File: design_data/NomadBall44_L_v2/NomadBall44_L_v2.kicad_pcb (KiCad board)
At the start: 2 copper layers, 149 x 96.5 mm, 58 parts, among them SW1 SW_Push, SW10 SW_Push, SW11 SW_Push, SW12 SW_Push, SW13 SW_Push, SW14 SW_Push, SW15 SW_Push, SW16 SW_Push, SW17 SW_Push, SW18 SW_Push, SW19 SW_Push, SW2 SW_Push, SW20 SW_Push, SW21 SW_Push, SW22 SW_Push, SW23 SW_Push, SW24 SW_SPDT, SW3 SW_Push, SW4 SW_Push, SW5 SW_Push, SW6 SW_Push, SW7 SW_Push, SW8 SW_Push, SW9 SW_Push, U1 XIAO-nRF52840-Plus-SMD

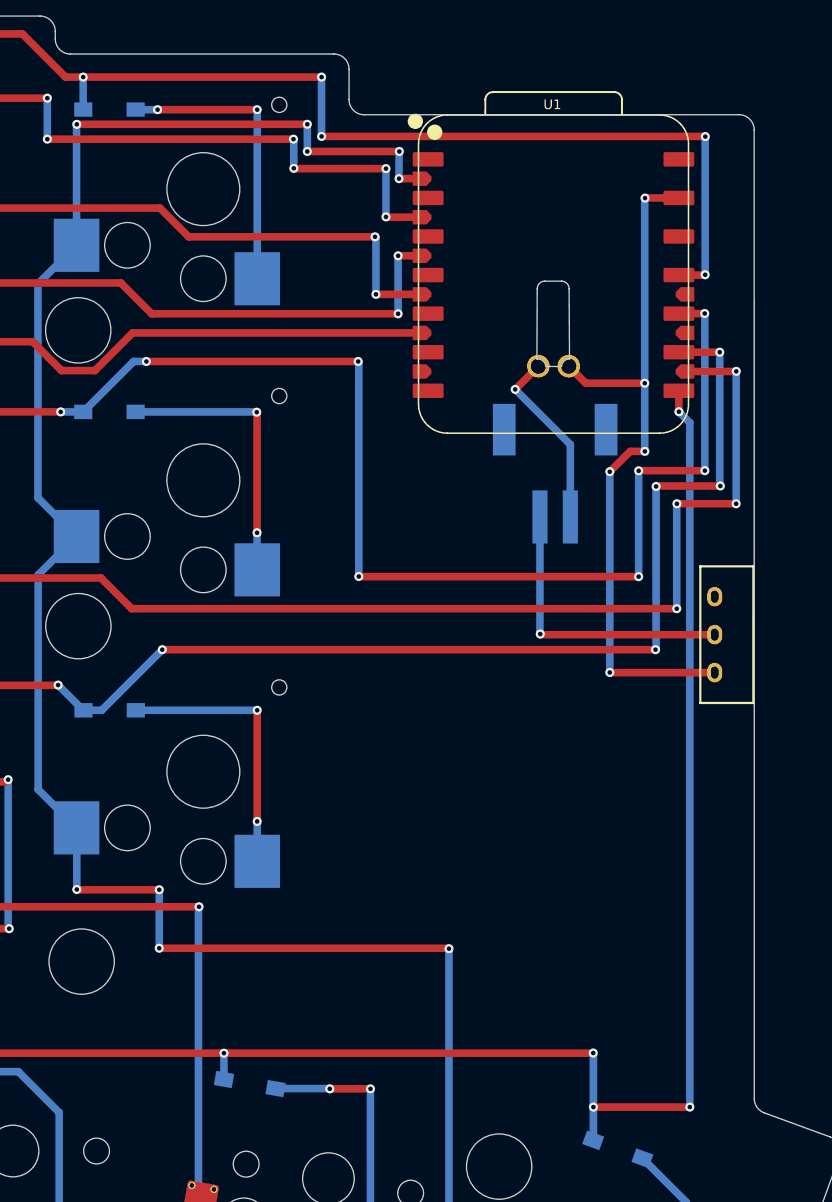
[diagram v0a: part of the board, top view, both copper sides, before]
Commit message: 左手基板のマイコンfootprintを変更し配線を修正
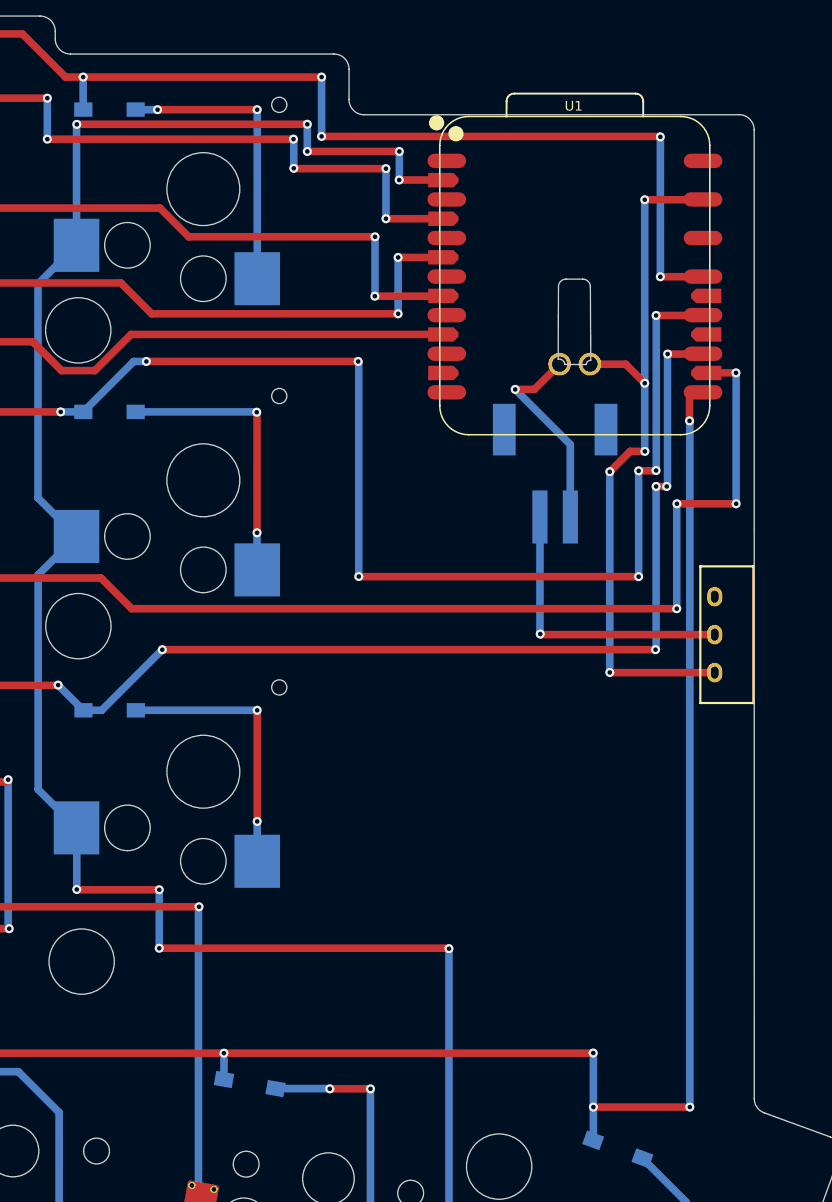
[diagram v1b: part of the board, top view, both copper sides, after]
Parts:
- U1: footprint NomadBall44:XIAO-nRF52840-Plus-ver2 -> NomadBall44:XIAO-nRF52840-Plus-ver3
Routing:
- net Row2: track 179.8 -> 175.0 mm
- net Row1: track 190.7 -> 188.0 mm
- net Row0: track 171.8 -> 169.2 mm
- net Col3: track 154.1 -> 155.7 mm
- net Col5: track 212.8 -> 211.3 mm
- net Col1: track 154.1 -> 155.6 mm
- net Col0: track 131.7 -> 133.3 mm
- net Bat: track 12.1 -> 13.5 mm
- net Col4: track 170.4 -> 171.8 mm
- net Col2: track 167.8 -> 169.1 mm
- net GND: track 47.4 -> 46.7 mm

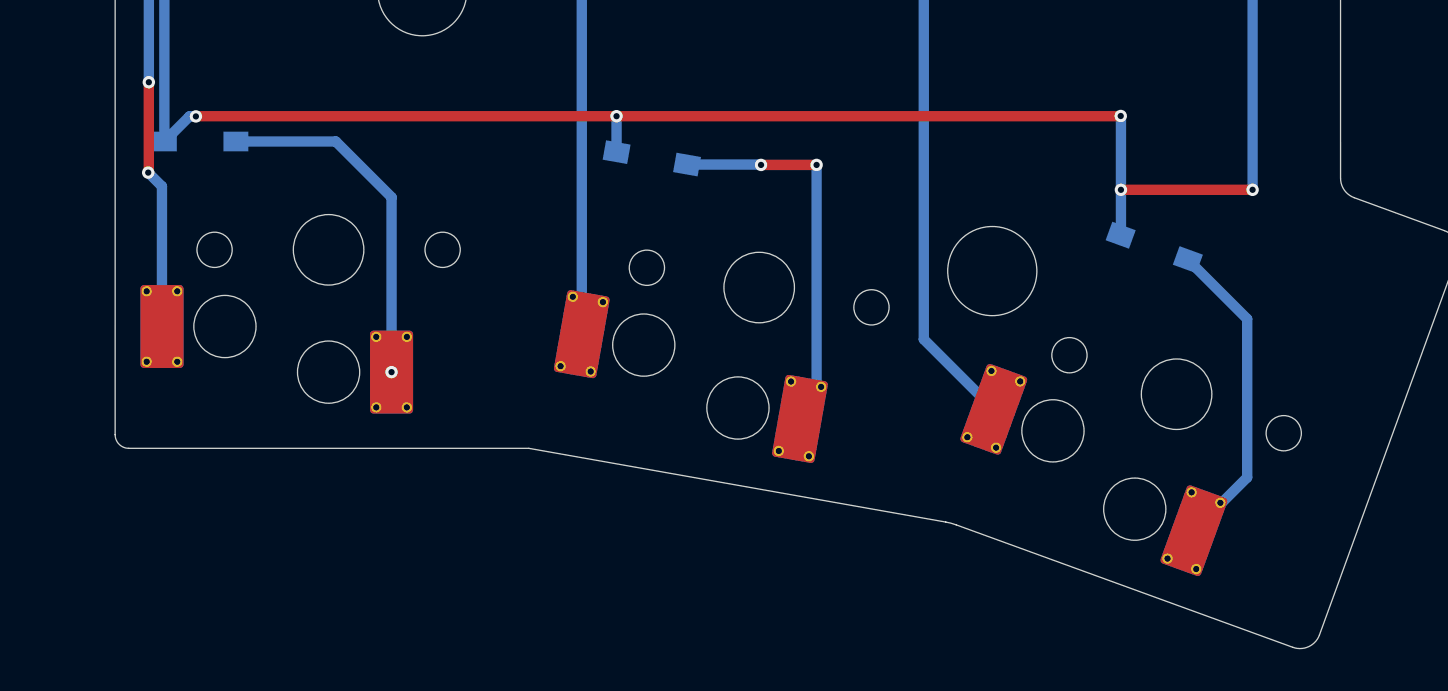
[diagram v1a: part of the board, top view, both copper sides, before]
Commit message: chocv1をchocv2に変更
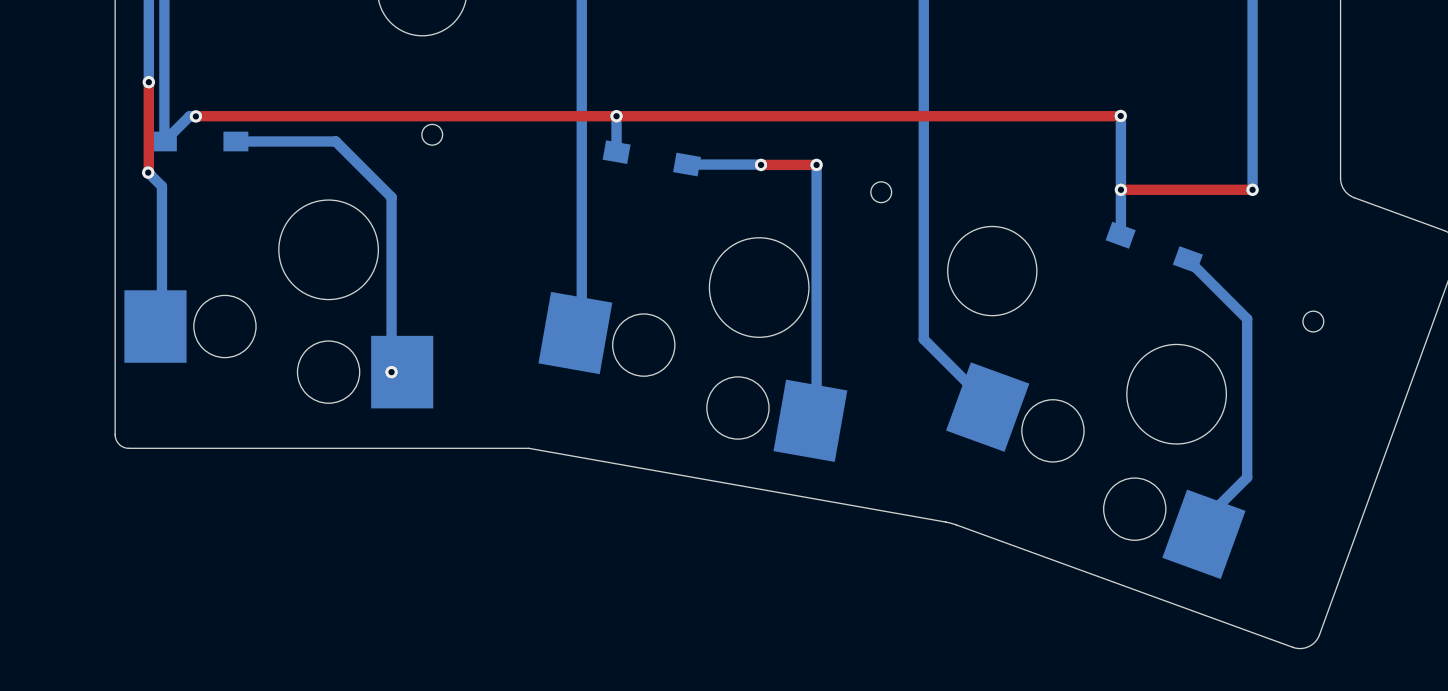
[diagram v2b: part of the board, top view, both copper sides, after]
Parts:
- SW19, SW20, SW21: footprint NomadBall44:Kailh_Choc_V1_Hotswap_thin_via -> NomadBall44:Choc_v2_Hotswap_1u

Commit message: キースイッチの配置を修正
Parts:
- renumbered SW6 to SW1, SW9 to SW10, SW8 to SW11, SW7 to SW12, SW18 to SW13, SW17 to SW14, SW16 to SW15, SW15 to SW16, SW14 to SW17, SW13 to SW18, SW23 to SW19, SW5 to SW2, SW22 to SW20, SW20 to SW22, SW19 to SW23, SW4 to SW3, SW3 to SW4, SW2 to SW5, SW1 to SW6, SW12 to SW7, SW11 to SW8, SW10 to SW9
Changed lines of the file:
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@@
 		(layer "F.Cu")
 		(at 181.384757 126.99)
-		(property "Reference" "SW22"
+		(property "Reference" "SW20"
 			(at 0.5 -5.5 180)
 			(layer "B.SilkS")
@@
 		(layer "F.Cu")
 		(at 162.284757 113.419999)
-		(property "Reference" "SW17"
+		(property "Reference" "SW14"
 			(at 0.5 -5.5 180)
 			(layer "B.SilkS")
@@
 		(layer "F.Cu")
 		(at 181.384757 107.789999)
-		(property "Reference" "SW16"
+		(property "Reference" "SW15"
 			(at 0.5 -5.5 180)
 			(layer "B.SilkS")
@@
 		(layer "F.Cu")
 		(at 247.190659 134.214444 -10)
-		(property "Reference" "SW20"
+		(property "Reference" "SW22"
 			(at 0.5 -5.5 170)
 			(layer "B.SilkS")
@@
 		)
 		(fp_line
-			(start -6.250001 6)
+			(start -6.250002 6)
 			(end -6.25 1.4)
 			(stroke
@@
 		(fp_line
 			(start -1.3 7.99)
-			(end -1.300001 3.6)
+			(end -1.300002 3.6)
 			(stroke
 				(width 0.15)
@@
 		)
 		(fp_line
-			(start 1.7 7.820001)
+			(start 1.7 7.820003)
 			(end 1.7 3.99)
 			(stroke
@@
 		)
 		(fp_line
-			(start 1.85 7.660001)
+			(start 1.85 7.660002)
 			(end 1.85 4.13)
 			(stroke
@@
 		(layer "F.Cu")
 		(at 143.10132 94.239999)
-		(property "Reference" "SW12"
+		(property "Reference" "SW7"
 			(at 0.5 -5.5 180)
 			(layer "B.SilkS")
@@
 		(layer "F.Cu")
 		(at 267.324757 139.359999 -20)
-		(property "Reference" "SW19"
+		(property "Reference" "SW23"
 			(at 0.5 -5.5 160)
 			(layer "B.SilkS")
@@
 		(fp_line
 			(start 0.95 8.2)
-			(end 0.95 3.600001)
+			(end 0.95 3.600002)
 			(stroke
 				(width 0.15)
@@
 		(layer "F.Cu")
 		(at 219.774757 85.989999)
-		(property "Reference" "SW8"
+		(property "Reference" "SW11"
 			(at 0.5 -5.5 180)
 			(layer "B.SilkS")
@@
 		(layer "F.Cu")
 		(at 200.584757 64.459999)
-		(property "Reference" "SW3"
+		(property "Reference" "SW4"
 			(at 0.5 -5.5 180)
 			(layer "B.SilkS")
@@
 		(layer "F.Cu")
 		(at 238.954132 107.414999)
-		(property "Reference" "SW13"
+		(property "Reference" "SW18"
 			(at 0.5 -5.5 180)
 			(layer "B.SilkS")
@@
 		(layer "F.Cu")
 		(at 219.774757 66.799999)
-		(property "Reference" "SW2"
+		(property "Reference" "SW5"
 			(at 0.5 -5.5 180)
 			(layer "B.SilkS")
@@
 		(layer "F.Cu")
 		(at 181.384757 88.644999)
-		(property "Reference" "SW10"
+		(property "Reference" "SW9"
 			(at 0.5 -5.5 180)
 			(layer "B.SilkS")
@@
 		(layer "F.Cu")
 		(at 143.10132 75.034999)
-		(property "Reference" "SW6"
+		(property "Reference" "SW1"
 			(at 0.5 -5.5 180)
 			(layer "B.SilkS")
@@
 		(layer "F.Cu")
 		(at 162.284757 75.034999)
-		(property "Reference" "SW5"
+		(property "Reference" "SW2"
 			(at 0.5 -5.5 180)
 			(layer "B.SilkS")
@@
 		(layer "F.Cu")
 		(at 200.584757 83.649999)
-		(property "Reference" "SW9"
+		(property "Reference" "SW10"
 			(at 0.5 -5.5 180)
 			(layer "B.SilkS")
@@
 		(layer "F.Cu")
 		(at 181.384757 69.449999)
-		(property "Reference" "SW4"
+		(property "Reference" "SW3"
 			(at 0.5 -5.5 180)
 			(layer "B.SilkS")
@@
 		(layer "F.Cu")
 		(at 143.10132 113.419999)
-		(property "Reference" "SW18"
+		(property "Reference" "SW13"
 			(at 0.5 -5.5 180)
 			(layer "B.SilkS")
@@
 		(layer "F.Cu")
 		(at 162.284757 132.469999)
-		(property "Reference" "SW23"
+		(property "Reference" "SW19"
 			(at 0.5 -5.5 180)
 			(layer "B.SilkS")
@@
 		(layer "F.Cu")
 		(at 238.954132 88.224999)
-		(property "Reference" "SW7"
+		(property "Reference" "SW12"
 			(at 0.5 -5.5 180)
 			(layer "B.SilkS")
@@
 		(layer "F.Cu")
 		(at 238.954132 69.049999)
-		(property "Reference" "SW1"
+		(property "Reference" "SW6"
 			(at 0.5 -5.5 180)
 			(layer "B.SilkS")
@@
 		(layer "F.Cu")
 		(at 162.284757 94.239999)
-		(property "Reference" "SW11"
+		(property "Reference" "SW8"
 			(at 0.5 -5.5 180)
 			(layer "B.SilkS")
@@
 		(layer "F.Cu")
 		(at 200.584757 102.814999)
-		(property "Reference" "SW15"
+		(property "Reference" "SW16"
 			(at 0.5 -5.5 180)
 			(layer "B.SilkS")
@@
 		(layer "F.Cu")
 		(at 219.774757 105.184999)
-		(property "Reference" "SW14"
+		(property "Reference" "SW17"
 			(at 0.5 -5.5 180)
 			(layer "B.SilkS")

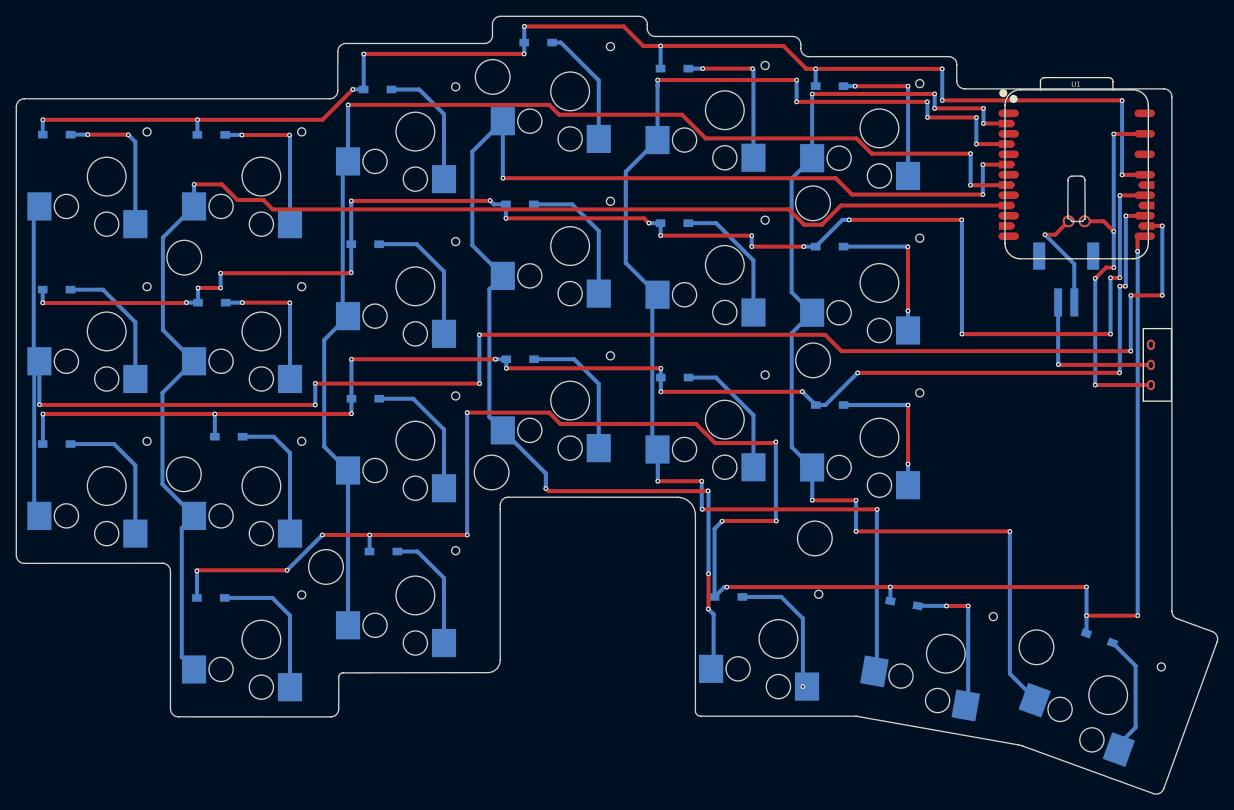
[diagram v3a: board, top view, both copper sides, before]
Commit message: ダイオードの配置を修正
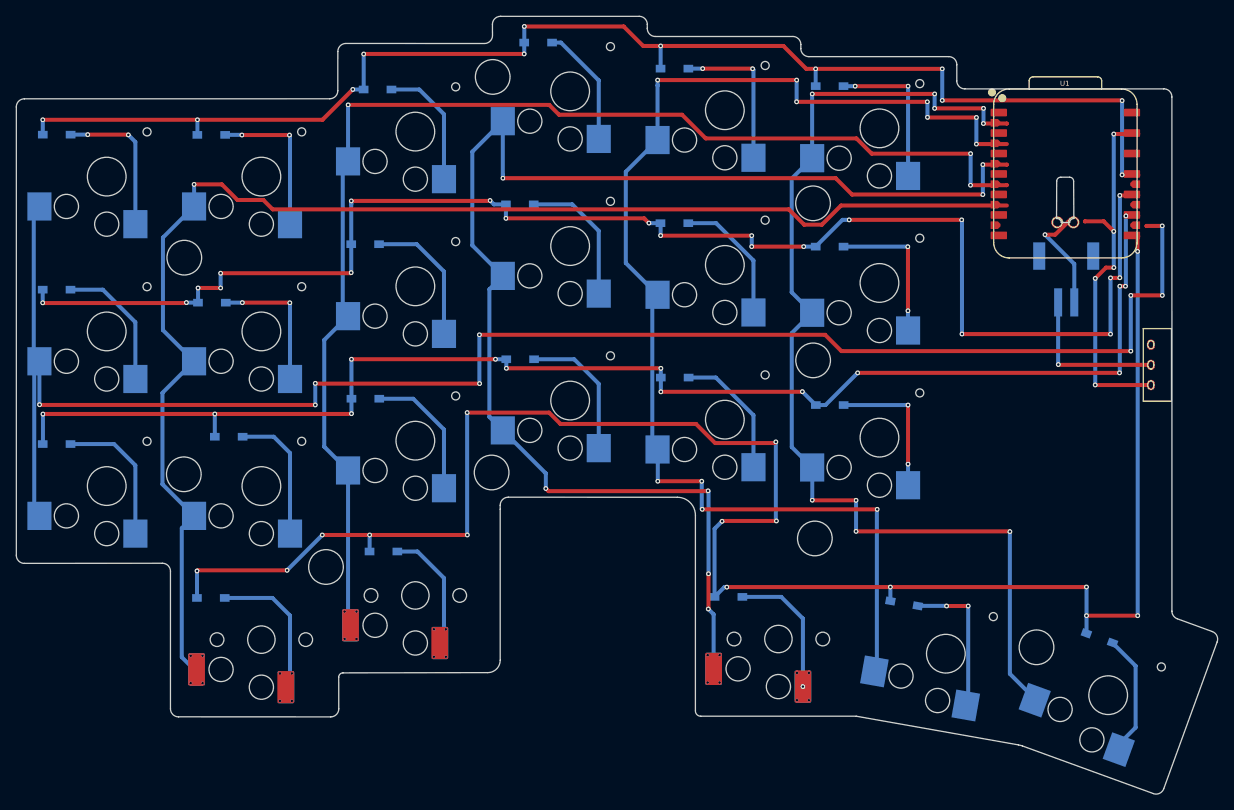
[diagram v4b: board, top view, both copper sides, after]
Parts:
- SW19, SW20, SW21: footprint NomadBall44:Choc_v2_Hotswap_1u -> NomadBall44:Kailh_Choc_V1_Hotswap_thin_via
- U1: footprint NomadBall44:XIAO-nRF52840-Plus-ver3 -> NomadBall44:XIAO-nRF52840-Plus-ver2
- renumbered D6 to D1, D9 to D10, D8 to D11, D7 to D12, D18 to D13, D17 to D14, D16 to D15, D15 to D16, D14 to D17, D13 to D18, D23 to D19, D5 to D2, D22 to D20, D20 to D22, D19 to D23, D4 to D3, D3 to D4, D2 to D5, D1 to D6, D12 to D7, D11 to D8, D10 to D9
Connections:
- SW1 pad 1: Col5 -> Col0
- SW10 pad 1: Col2 -> Col3
- SW11 pad 1: Col1 -> Col4
- SW12 pad 1: Col0 -> Col5
- SW13 pad 1: Col5 -> Col0
- SW14 pad 1: Col4 -> Col1
- SW15 pad 1: Col3 -> Col2
- SW16 pad 1: Col2 -> Col3
- SW17 pad 1: Col1 -> Col4
- SW18 pad 1: Col0 -> Col5
- SW19 pad 1: Col4 -> Col0
- SW2 pad 1: Col4 -> Col1
- SW20 pad 1: Col3 -> Col1
- SW22 pad 1: Col1 -> Col3
- SW23 pad 1: Col0 -> Col4
- SW3 pad 1: Col3 -> Col2
- SW4 pad 1: Col2 -> Col3
- SW5 pad 1: Col1 -> Col4
- SW6 pad 1: Col0 -> Col5
- SW7 pad 1: Col5 -> Col0
- SW8 pad 1: Col4 -> Col1
- SW9 pad 1: Col3 -> Col2
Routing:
- net Col5: track 211.3 -> 0.00 mm, vias 9 -> 0
- net Col0: track 133.3 -> 344.5 mm, vias 9 -> 18

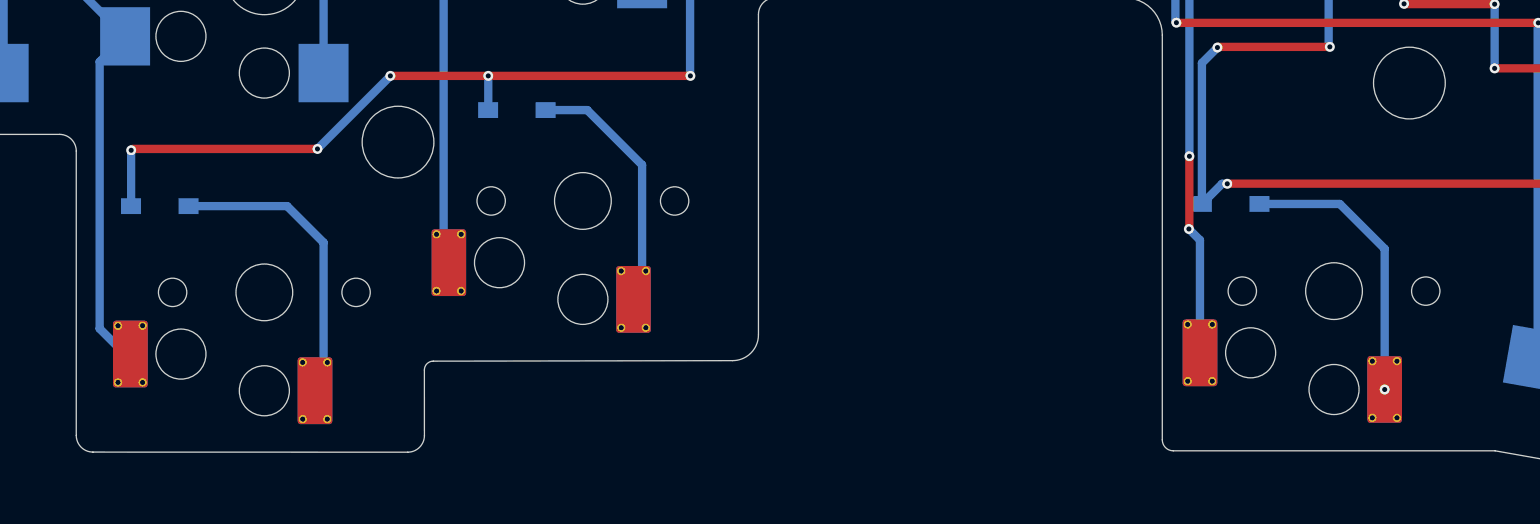
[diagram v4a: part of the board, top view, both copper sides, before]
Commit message: キースイッチをchocv1からchocv2へ変更
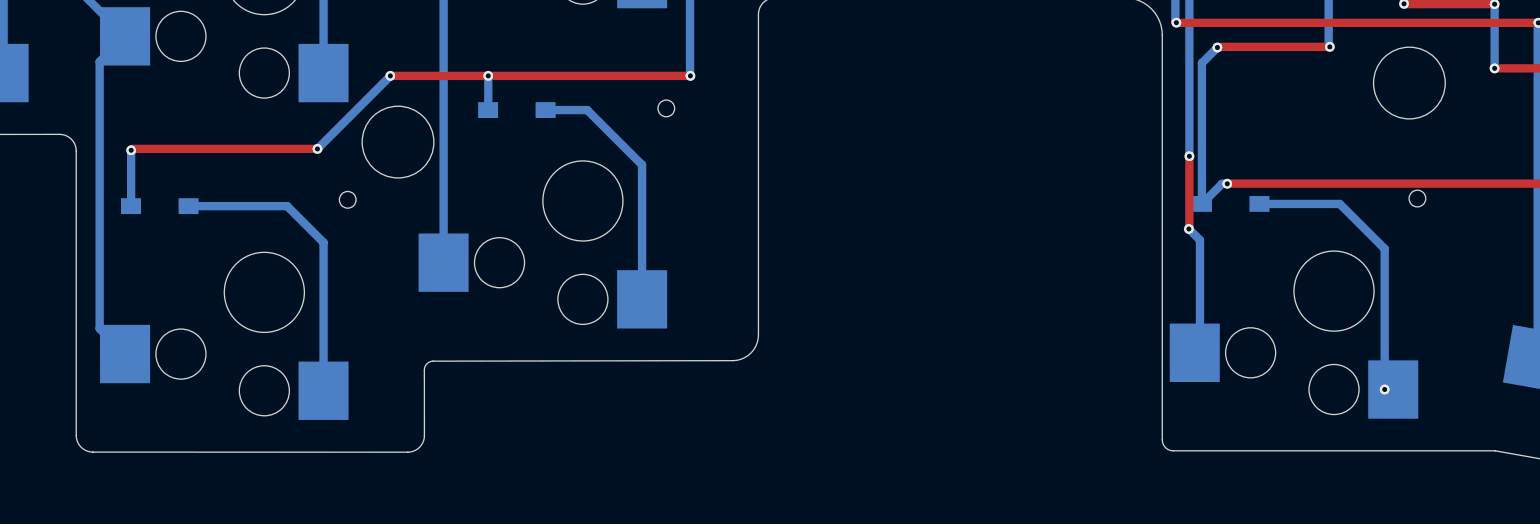
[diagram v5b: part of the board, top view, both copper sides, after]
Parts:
- SW19, SW20, SW21: footprint NomadBall44:Kailh_Choc_V1_Hotswap_thin_via -> NomadBall44:Choc_v2_Hotswap_1u
